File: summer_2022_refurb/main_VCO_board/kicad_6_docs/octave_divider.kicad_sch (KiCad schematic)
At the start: 10 parts

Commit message: Main VCO progress
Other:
- title: (none) -> Josh Ox Ribon Synth Main VCO board
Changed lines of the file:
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@@
 (kicad_sch (version 20211123) (generator eeschema)
   (paper "A4")
+  (title_block
+    (title "Josh Ox Ribon Synth Main VCO board")
+    (date "2022-06-18")
+    (rev "0")
+    (comment 2 "creativecommons.org/licences/by/4.0")
+    (comment 3 "license: CC by 4.0")
+    (comment 4 "Author: Jordan Acete")
+  )
   (junction (at 128.27 64.77) (diameter 0) (color 0 0 0 0)
   )

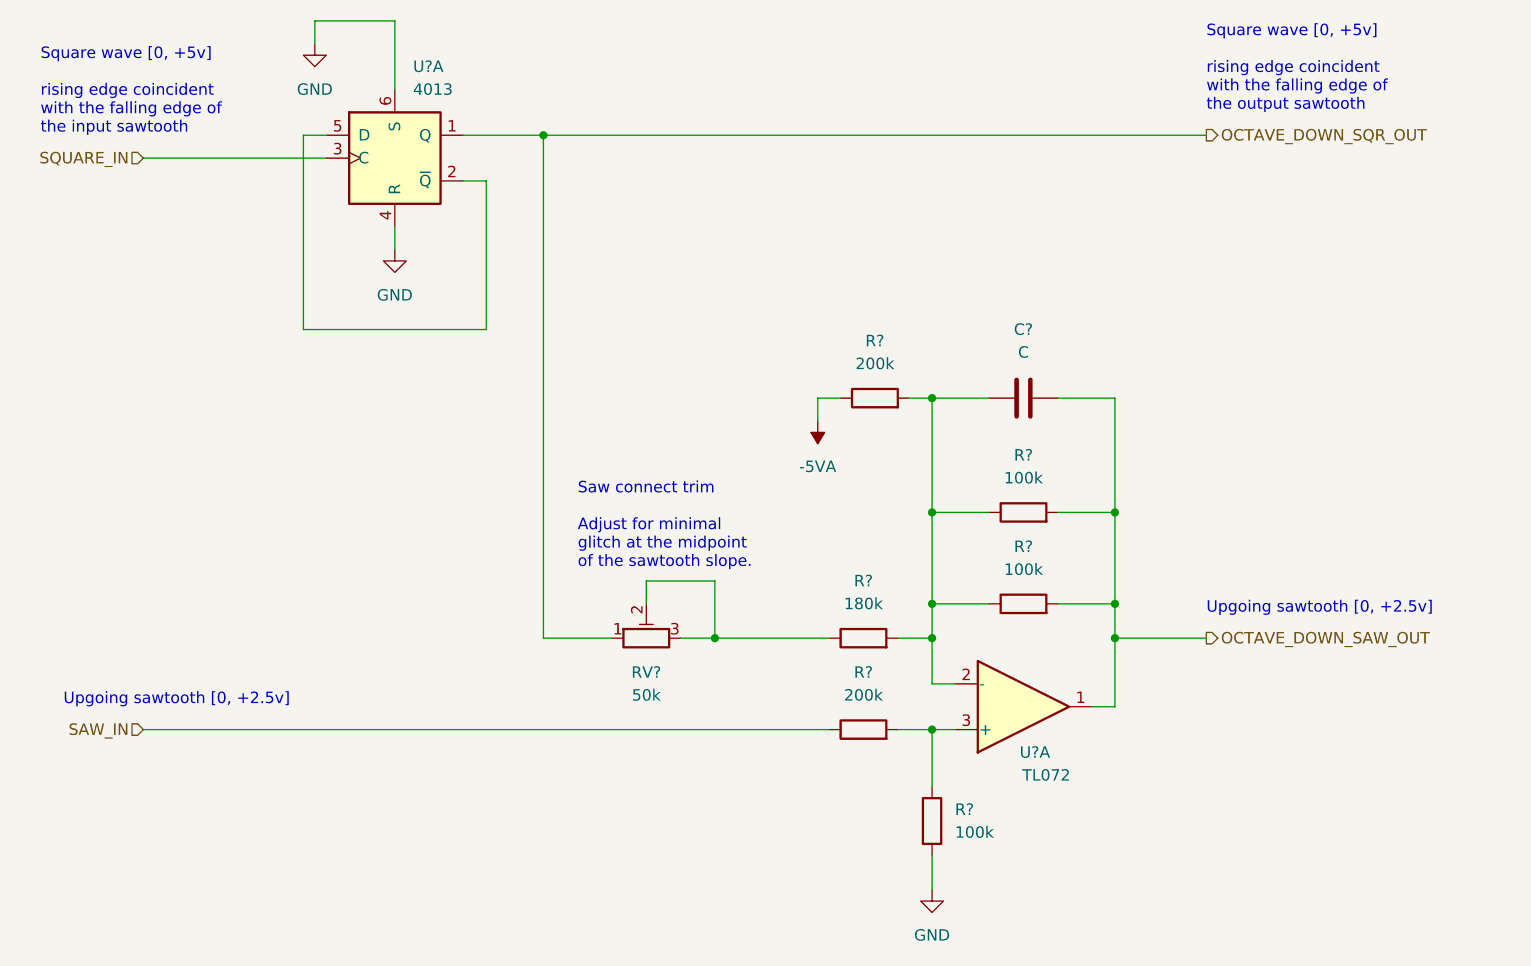
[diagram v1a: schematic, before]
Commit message: Progress on main VCO, schem getting close but not done
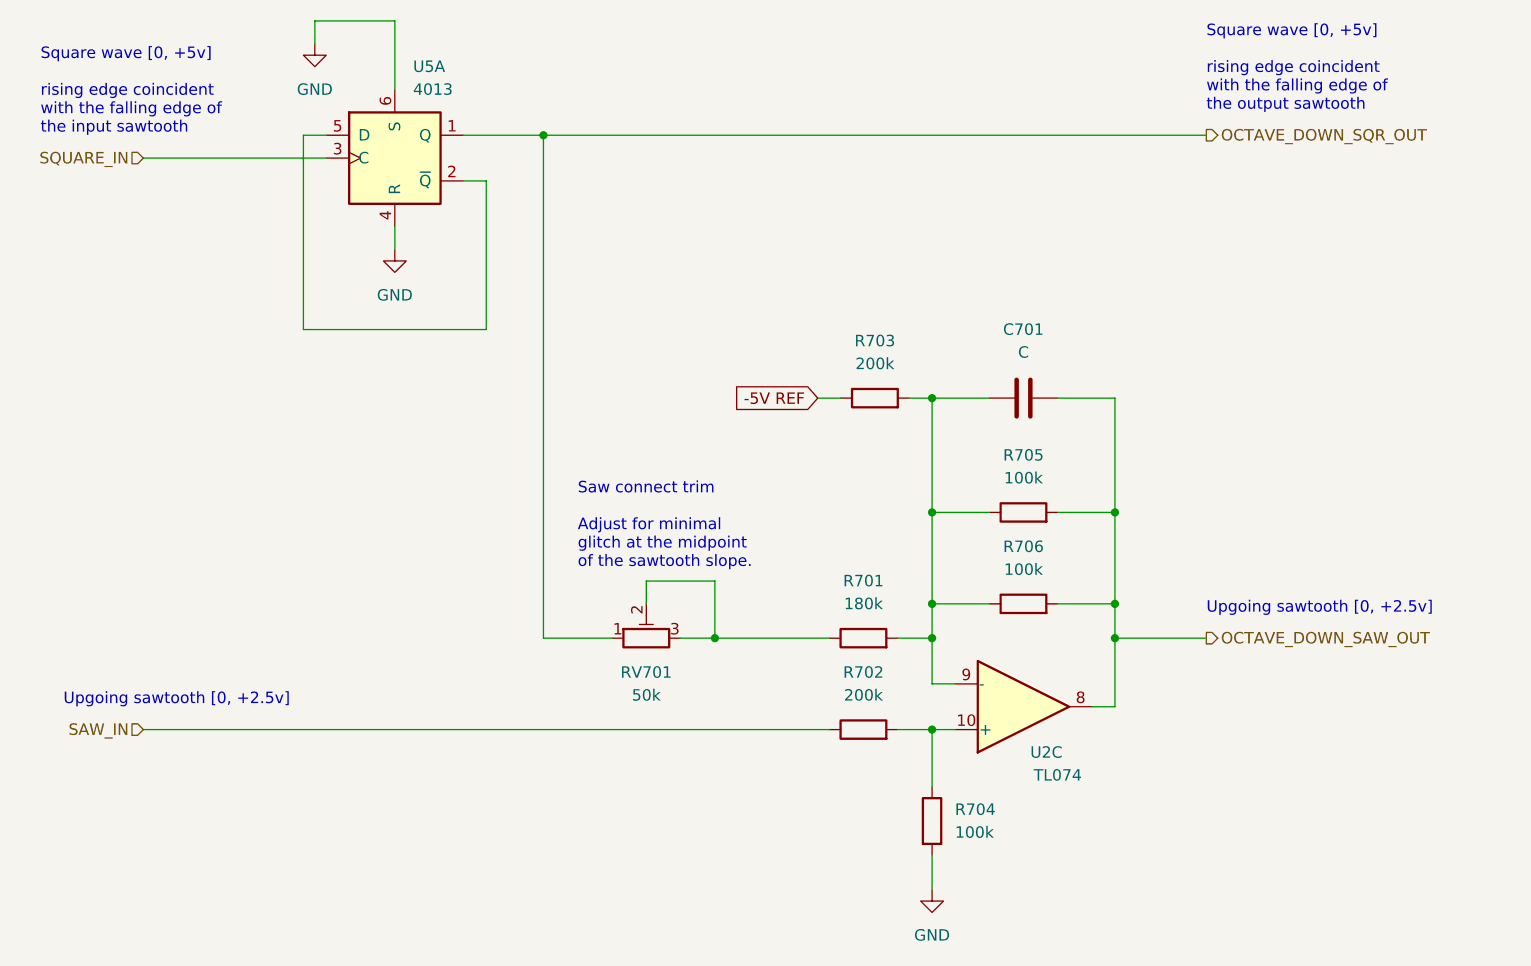
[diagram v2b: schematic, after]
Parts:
- removed U?: TL072, symbol Amplifier_Operational:TL072
- added U2: TL074, symbol Amplifier_Operational:TL074
- gave numbers to parts that had none: 9
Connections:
- net OCTAVE_DOWN_SAW_OUT: now also U2.8
- net at C701.1, R701.2, R703.2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: now also U2.9 (-)
- net at R702.2, R704.1: now also U2.10 (+)
- net -5VA renamed -5V REF
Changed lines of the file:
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@@
-    (stroke (width 0) (type default) (color 0 0 0 0))
-  )
-  (wire (pts (xy 158.75 93.98) (xy 158.75 96.52))
     (stroke (width 0) (type default) (color 0 0 0 0))
   )
@@
     (effects (font (size 1.27 1.27)) (justify left bottom))
   )
+  (global_label "-5V REF" (shape input) (at 158.75 93.98 180) (fields_autoplaced)
+    (effects (font (size 1.27 1.27)) (justify right))
+    (property "Intersheet References" "${INTERSHEET_REFS}" (id 0) (at 147.9912 93.9006 0)
+      (effects (font (size 1.27 1.27)) (justify right) hide)
+    )
+  )
   (hierarchical_label "SAW_IN" (shape input) (at 83.82 130.81 180)
     (effects (font (size 1.27 1.27)) (justify right))
@@
   (symbol (lib_id "Device:R") (at 165.1 93.98 90) (unit 1)
     (in_bom yes) (on_board yes) (fields_autoplaced)
-    (property "Reference" "R?" (id 0) (at 165.1 87.63 90))
+    (property "Reference" "R703" (id 0) (at 165.1 87.63 90))
     (property "Value" "200k" (id 1) (at 165.1 90.17 90))
     (property "Footprint" "" (id 2) (at 165.1 95.758 90)
@@
   (symbol (lib_id "power:GND") (at 102.87 54.61 0) (unit 1)
     (in_bom yes) (on_board yes) (fields_autoplaced)
-    (property "Reference" "#PWR?" (id 0) (at 102.87 60.96 0)
+    (property "Reference" "#PWR0701" (id 0) (at 102.87 60.96 0)
       (effects (font (size 1.27 1.27)) hide)
     )
@@
   (symbol (lib_id "power:GND") (at 111.76 77.47 0) (unit 1)
     (in_bom yes) (on_board yes) (fields_autoplaced)
-    (property "Reference" "#PWR?" (id 0) (at 111.76 83.82 0)
+    (property "Reference" "#PWR0702" (id 0) (at 111.76 83.82 0)
       (effects (font (size 1.27 1.27)) hide)
     )
@@
   (symbol (lib_id "Device:R") (at 163.83 120.65 90) (unit 1)
     (in_bom yes) (on_board yes) (fields_autoplaced)
-    (property "Reference" "R?" (id 0) (at 163.83 114.3 90))
+    (property "Reference" "R701" (id 0) (at 163.83 114.3 90))
     (property "Value" "180k" (id 1) (at 163.83 116.84 90))
     (property "Footprint" "" (id 2) (at 163.83 122.428 90)
@@
   (symbol (lib_id "Device:R") (at 181.61 106.68 90) (unit 1)
     (in_bom yes) (on_board yes)
-    (property "Reference" "R?" (id 0) (at 181.61 100.33 90))
+    (property "Reference" "R705" (id 0) (at 181.61 100.33 90))
     (property "Value" "100k" (id 1) (at 181.61 102.87 90))
     (property "Footprint" "" (id 2) (at 181.61 108.458 90)
@@
   (symbol (lib_id "Device:C") (at 181.61 93.98 90) (unit 1)
     (in_bom yes) (on_board yes) (fields_autoplaced)
-    (property "Reference" "C?" (id 0) (at 181.61 86.36 90))
+    (property "Reference" "C701" (id 0) (at 181.61 86.36 90))
     (property "Value" "C" (id 1) (at 181.61 88.9 90))
     (property "Footprint" "" (id 2) (at 185.42 93.0148 0)
@@
   (symbol (lib_id "Device:R") (at 171.45 140.97 0) (unit 1)
     (in_bom yes) (on_board yes) (fields_autoplaced)
-    (property "Reference" "R?" (id 0) (at 173.99 139.6999 0)
+    (property "Reference" "R704" (id 0) (at 173.99 139.6999 0)
       (effects (font (size 1.27 1.27)) (justify left))
     )
@@
   (symbol (lib_id "4xxx:4013") (at 111.76 67.31 0) (unit 1)
     (in_bom yes) (on_board yes)
-    (property "Reference" "U?" (id 0) (at 113.7794 57.15 0)
+    (property "Reference" "U5" (id 0) (at 113.7794 57.15 0)
       (effects (font (size 1.27 1.27)) (justify left))
     )
@@
   (symbol (lib_id "power:GND") (at 171.45 148.59 0) (unit 1)
     (in_bom yes) (on_board yes) (fields_autoplaced)
-    (property "Reference" "#PWR?" (id 0) (at 171.45 154.94 0)
+    (property "Reference" "#PWR0704" (id 0) (at 171.45 154.94 0)
       (effects (font (size 1.27 1.27)) hide)
     )
@@
     (pin "1")
   )
-  (symbol (lib_id "Device:R_Potentiometer_Trim") (at 139.7 120.65 90) (unit 1)
-    (in_bom yes) (on_board yes) (fields_autoplaced)
-    (property "Reference" "RV?" (id 0) (at 139.7 124.46 90))
-    (property "Value" "50k" (id 1) (at 139.7 127 90))
-    (property "Footprint" "" (id 2) (at 139.7 120.65 0)
-      (effects (font (size 1.27 1.27)) hide)
-    )
-    (property "Datasheet" "~" (id 3) (at 139.7 120.65 0)
-      (effects (font (size 1.27 1.27)) hide)
-    )
-    (pin "1")
-    (pin "2")
-    (pin "3")
-  )
-  (symbol (lib_id "Device:R") (at 181.61 116.84 90) (unit 1)
+  (symbol (lib_id "Amplifier_Operational:TL074") (at 181.61 128.27 0) (mirror x) (unit 3)
     (in_bom yes) (on_board yes)
-    (property "Reference" "R?" (id 0) (at 181.61 110.49 90))
-    (property "Value" "100k" (id 1) (at 181.61 113.03 90))
-    (property "Footprint" "" (id 2) (at 181.61 118.618 90)
-      (effects (font (size 1.27 1.27)) hide)
-    )
-    (property "Datasheet" "~" (id 3) (at 181.61 116.84 0)
-      (effects (font (size 1.27 1.27)) hide)
-    )
-    (pin "1")
-    (pin "2")
-  )
-  (symbol (lib_id "power:-5VA") (at 158.75 96.52 180) (unit 1)
-    (in_bom yes) (on_board yes) (fields_autoplaced)
-    (property "Reference" "#PWR?" (id 0) (at 158.75 99.06 0)
-      (effects (font (size 1.27 1.27)) hide)
-    )
-    (property "Value" "-5VA" (id 1) (at 158.75 101.6 0))
-    (property "Footprint" "" (id 2) (at 158.75 96.52 0)
-      (effects (font (size 1.27 1.27)) hide)
-    )
-    (property "Datasheet" "" (id 3) (at 158.75 96.52 0)
-      (effects (font (size 1.27 1.27)) hide)
-    )
-    (pin "1")
-  )
-  (symbol (lib_id "Device:R") (at 163.83 130.81 90) (unit 1)
-    (in_bom yes) (on_board yes) (fields_autoplaced)
-    (property "Reference" "R?" (id 0) (at 163.83 124.46 90))
-    (property "Value" "200k" (id 1) (at 163.83 127 90))
-    (property "Footprint" "" (id 2) (at 163.83 132.588 90)
-      (effects (font (size 1.27 1.27)) hide)
-    )
-    (property "Datasheet" "~" (id 3) (at 163.83 130.81 0)
-      (effects (font (size 1.27 1.27)) hide)
-    )
-    (pin "1")
-    (pin "2")
-  )
-  (symbol (lib_id "Amplifier_Operational:TL072") (at 181.61 128.27 0) (mirror x) (unit 1)
-    (in_bom yes) (on_board yes)
-    (property "Reference" "U?" (id 0) (at 182.88 133.35 0))
-    (property "Value" "TL072" (id 1) (at 184.15 135.89 0))
-    (property "Footprint" "" (id 2) (at 181.61 128.27 0)
-      (effects (font (size 1.27 1.27)) hide)
-    )
-    (property "Datasheet" "http://www.ti.com/lit/ds/symlink/tl071.pdf" (id 3) (at 181.61 128.27 0)
+    (property "Reference" "U2" (id 0) (at 184.15 133.35 0))
+    (property "Value" "TL074" (id 1) (at 185.42 135.89 0))
+    (property "Footprint" "" (id 2) (at 180.34 130.81 0)
+      (effects (font (size 1.27 1.27)) hide)
+    )
+    (property "Datasheet" "http://www.ti.com/lit/ds/symlink/tl071.pdf" (id 3) (at 182.88 133.35 0)
       (effects (font (size 1.27 1.27)) hide)
     )
@@
     (pin "6")
     (pin "7")
+    (pin "10")
+    (pin "8")
+    (pin "9")
+    (pin "12")
+    (pin "13")
+    (pin "14")
+    (pin "11")
     (pin "4")
-    (pin "8")
+  )
+  (symbol (lib_id "Device:R_Potentiometer_Trim") (at 139.7 120.65 90) (unit 1)
+    (in_bom yes) (on_board yes) (fields_autoplaced)
+    (property "Reference" "RV701" (id 0) (at 139.7 124.46 90))
+    (property "Value" "50k" (id 1) (at 139.7 127 90))
+    (property "Footprint" "" (id 2) (at 139.7 120.65 0)
+      (effects (font (size 1.27 1.27)) hide)
+    )
+    (property "Datasheet" "~" (id 3) (at 139.7 120.65 0)
+      (effects (font (size 1.27 1.27)) hide)
+    )
+    (pin "1")
+    (pin "2")
+    (pin "3")
+  )
+  (symbol (lib_id "Device:R") (at 181.61 116.84 90) (unit 1)
+    (in_bom yes) (on_board yes)
+    (property "Reference" "R706" (id 0) (at 181.61 110.49 90))
+    (property "Value" "100k" (id 1) (at 181.61 113.03 90))
+    (property "Footprint" "" (id 2) (at 181.61 118.618 90)
+      (effects (font (size 1.27 1.27)) hide)
+    )
+    (property "Datasheet" "~" (id 3) (at 181.61 116.84 0)
+      (effects (font (size 1.27 1.27)) hide)
+    )
+    (pin "1")
+    (pin "2")
+  )
+  (symbol (lib_id "Device:R") (at 163.83 130.81 90) (unit 1)
+    (in_bom yes) (on_board yes) (fields_autoplaced)
+    (property "Reference" "R702" (id 0) (at 163.83 124.46 90))
+    (property "Value" "200k" (id 1) (at 163.83 127 90))
+    (property "Footprint" "" (id 2) (at 163.83 132.588 90)
+      (effects (font (size 1.27 1.27)) hide)
+    )
+    (property "Datasheet" "~" (id 3) (at 163.83 130.81 0)
+      (effects (font (size 1.27 1.27)) hide)
+    )
+    (pin "1")
+    (pin "2")
   )
 )

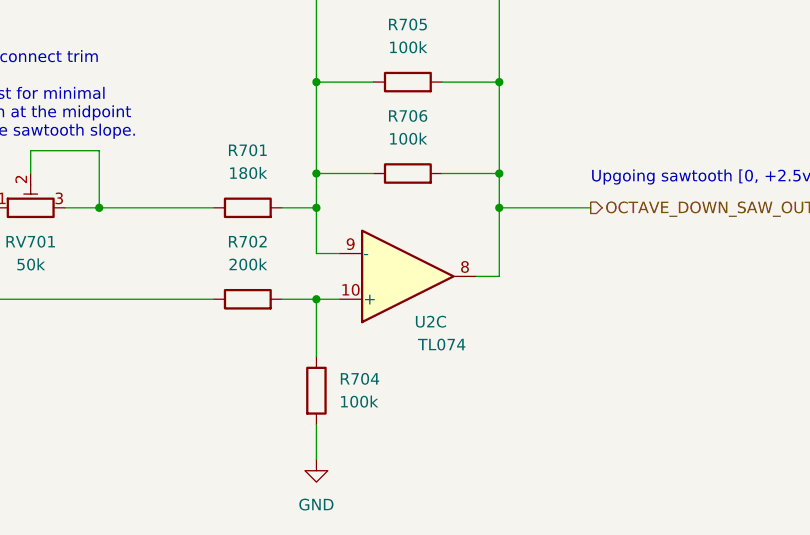
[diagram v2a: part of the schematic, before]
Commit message: Main VCO rough parts placement
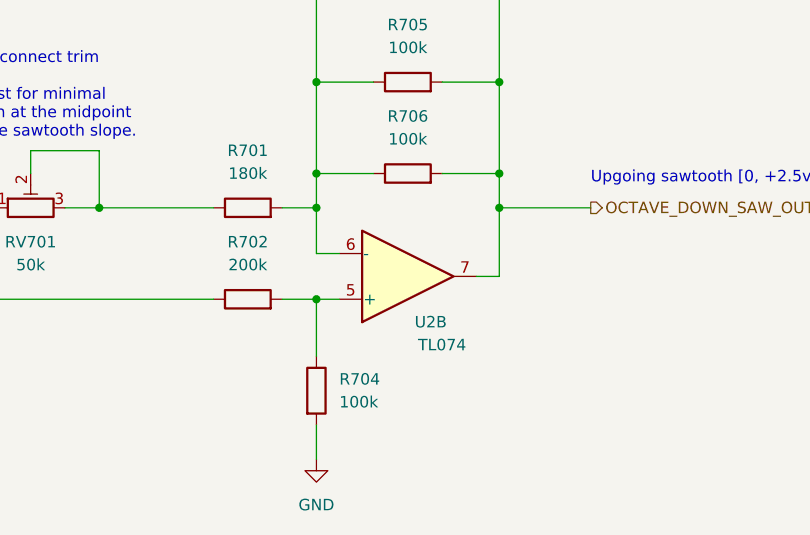
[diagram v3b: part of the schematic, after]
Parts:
- C701: footprint (none) -> Capacitor_SMD:C_0805_2012Metric
- R701, R702, R703, R704, R705, R706: footprint (none) -> Resistor_SMD:R_0805_2012Metric
- RV701: footprint (none) -> Potentiometer_THT:Potentiometer_Bourns_3296W_Vertical
- U2, U5: footprint (none) -> Package_SO:SOIC-14_3.9x8.7mm_P1.27mm
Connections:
- net OCTAVE_DOWN_SAW_OUT: now also U2.7; no longer U2.8
- net at C701.1, R701.2, R703.2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: now also U2.6 (-); no longer U2.9 (-)
- net at R702.2, R704.1: now also U2.5 (+); no longer U2.10 (+)
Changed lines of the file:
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@@
     (property "Reference" "R703" (id 0) (at 165.1 87.63 90))
     (property "Value" "200k" (id 1) (at 165.1 90.17 90))
-    (property "Footprint" "" (id 2) (at 165.1 95.758 90)
+    (property "Footprint" "Resistor_SMD:R_0805_2012Metric" (id 2) (at 165.1 95.758 90)
       (effects (font (size 1.27 1.27)) hide)
     )
@@
     (property "Reference" "R701" (id 0) (at 163.83 114.3 90))
     (property "Value" "180k" (id 1) (at 163.83 116.84 90))
-    (property "Footprint" "" (id 2) (at 163.83 122.428 90)
+    (property "Footprint" "Resistor_SMD:R_0805_2012Metric" (id 2) (at 163.83 122.428 90)
       (effects (font (size 1.27 1.27)) hide)
     )
@@
     (property "Reference" "R705" (id 0) (at 181.61 100.33 90))
     (property "Value" "100k" (id 1) (at 181.61 102.87 90))
-    (property "Footprint" "" (id 2) (at 181.61 108.458 90)
+    (property "Footprint" "Resistor_SMD:R_0805_2012Metric" (id 2) (at 181.61 108.458 90)
       (effects (font (size 1.27 1.27)) hide)
     )
@@
     (property "Reference" "C701" (id 0) (at 181.61 86.36 90))
     (property "Value" "C" (id 1) (at 181.61 88.9 90))
-    (property "Footprint" "" (id 2) (at 185.42 93.0148 0)
+    (property "Footprint" "Capacitor_SMD:C_0805_2012Metric" (id 2) (at 185.42 93.0148 0)
       (effects (font (size 1.27 1.27)) hide)
     )
@@
       (effects (font (size 1.27 1.27)) (justify left))
     )
-    (property "Footprint" "" (id 2) (at 169.672 140.97 90)
+    (property "Footprint" "Resistor_SMD:R_0805_2012Metric" (id 2) (at 169.672 140.97 90)
       (effects (font (size 1.27 1.27)) hide)
     )
@@
       (effects (font (size 1.27 1.27)) (justify left))
     )
-    (property "Footprint" "" (id 2) (at 111.76 67.31 0)
+    (property "Footprint" "Package_SO:SOIC-14_3.9x8.7mm_P1.27mm" (id 2) (at 111.76 67.31 0)
       (effects (font (size 1.27 1.27)) hide)
     )
@@
     (pin "1")
   )
-  (symbol (lib_id "Amplifier_Operational:TL074") (at 181.61 128.27 0) (mirror x) (unit 3)
+  (symbol (lib_id "Amplifier_Operational:TL074") (at 181.61 128.27 0) (mirror x) (unit 2)
     (in_bom yes) (on_board yes)
     (property "Reference" "U2" (id 0) (at 184.15 133.35 0))
     (property "Value" "TL074" (id 1) (at 185.42 135.89 0))
-    (property "Footprint" "" (id 2) (at 180.34 130.81 0)
+    (property "Footprint" "Package_SO:SOIC-14_3.9x8.7mm_P1.27mm" (id 2) (at 180.34 130.81 0)
       (effects (font (size 1.27 1.27)) hide)
     )
@@
     (property "Reference" "RV701" (id 0) (at 139.7 124.46 90))
     (property "Value" "50k" (id 1) (at 139.7 127 90))
-    (property "Footprint" "" (id 2) (at 139.7 120.65 0)
+    (property "Footprint" "Potentiometer_THT:Potentiometer_Bourns_3296W_Vertical" (id 2) (at 139.7 120.65 0)
       (effects (font (size 1.27 1.27)) hide)
     )
@@
     (property "Reference" "R706" (id 0) (at 181.61 110.49 90))
     (property "Value" "100k" (id 1) (at 181.61 113.03 90))
-    (property "Footprint" "" (id 2) (at 181.61 118.618 90)
+    (property "Footprint" "Resistor_SMD:R_0805_2012Metric" (id 2) (at 181.61 118.618 90)
       (effects (font (size 1.27 1.27)) hide)
     )
@@
     (property "Reference" "R702" (id 0) (at 163.83 124.46 90))
     (property "Value" "200k" (id 1) (at 163.83 127 90))
-    (property "Footprint" "" (id 2) (at 163.83 132.588 90)
+    (property "Footprint" "Resistor_SMD:R_0805_2012Metric" (id 2) (at 163.83 132.588 90)
       (effects (font (size 1.27 1.27)) hide)
     )
